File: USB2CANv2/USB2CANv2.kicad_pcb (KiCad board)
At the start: 2 copper layers, 53 parts, among them IC1 MIC5528-3.3YMT-TR, J1 USB_C_Receptacle_USB2.0, J3 Conn_01x04_Pin, SW1 SW_BOOT0, U1 STM32F405RGTx, U2 USBLC6-2P6, U3 MCP2561-E-SN, U4 TLP175A, U5 MCP2561-E-SN, U6 TLP175A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

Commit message: Creating PCB
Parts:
- added J2: Conn_01x06_Pin, IDC:IDC_SMD_3PIN, F.Cu at (96.0, 117.3)
- added J4: Conn_01x02_Pin, Connector_PinHeader_2.54mm:PinHeader_1x02_P2.54mm_Vertical, F.Cu at (54.1, 108.7)
- added J5: Conn_01x02_Pin, Connector_PinHeader_2.54mm:PinHeader_1x02_P2.54mm_Vertical, F.Cu at (54.4, 125.2)
- added R15: 0, Resistor_SMD:R_0402_1005Metric_Pad0.72x0.64mm_HandSolder, F.Cu at (132.5, 57.0)
- added R16: 0, Resistor_SMD:R_0402_1005Metric_Pad0.72x0.64mm_HandSolder, F.Cu at (132.5, 59.0)
- added R17: 0, Resistor_SMD:R_0402_1005Metric_Pad0.72x0.64mm_HandSolder, F.Cu at (132.5, 61.0)
- added R18: 0, Resistor_SMD:R_0402_1005Metric_Pad0.72x0.64mm_HandSolder, F.Cu at (132.5, 63.0)
- added TP1: TestPoint, TestPoint:TestPoint_Pad_1.5x1.5mm, B.Cu at (76.7, 126.0)
- added TP2: TestPoint, TestPoint:TestPoint_Pad_1.5x1.5mm, B.Cu at (69.1, 126.0)
- added TP3: TestPoint, TestPoint:TestPoint_Pad_1.5x1.5mm, B.Cu at (71.6, 126.0)
- added TP4: TestPoint, TestPoint:TestPoint_Pad_1.5x1.5mm, B.Cu at (74.2, 126.0)
- IC1, U3, U4, U5, U6: moved to B.Cu
- J3: value Conn_01x04_Pin -> Conn_01x02_Pin; footprint Connector_PinHeader_2.54mm:PinHeader_1x01_P2.54mm_Vertical -> Connector_PinHeader_2.00mm:PinHeader_1x02_P2.00mm_Vertical
- moved D1 94.5 mm to (59.5, 125.2)
- moved D3 85.0 mm to (49.8, 113.5), turned to -90 degrees
- moved U3 82.8 mm to (66.5, 120.4), turned to 180 degrees
- moved U4 79.6 mm to (54.4, 119.1), turned to 180 degrees
- moved D2 77.6 mm to (59.8, 108.7)
- moved J1 74.3 mm to (44.2, 113.9), turned to -90 degrees
- moved H3 74.1 mm to (96.5, 124.5)
- moved U6 71.4 mm to (54.4, 113.3), turned to 180 degrees
- moved U1 70.3 mm to (73.4, 116.7), turned to 180 degrees
- moved U5 69.5 mm to (66.5, 112.3), turned to 180 degrees
- moved Y2 68.3 mm to (58.9, 119.4)
- moved D4 61.9 mm to (80.3, 108.2)
- moved SW1 56.1 mm to (85.3, 124.5)
- moved H4 54.7 mm to (96.5, 109.2)
- moved IC1 54.6 mm to (82.8, 115.8), turned to 180 degrees
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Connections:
- J3 pad 1: GND -> +5V
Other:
- board outline added: 61 x 20.3 mm

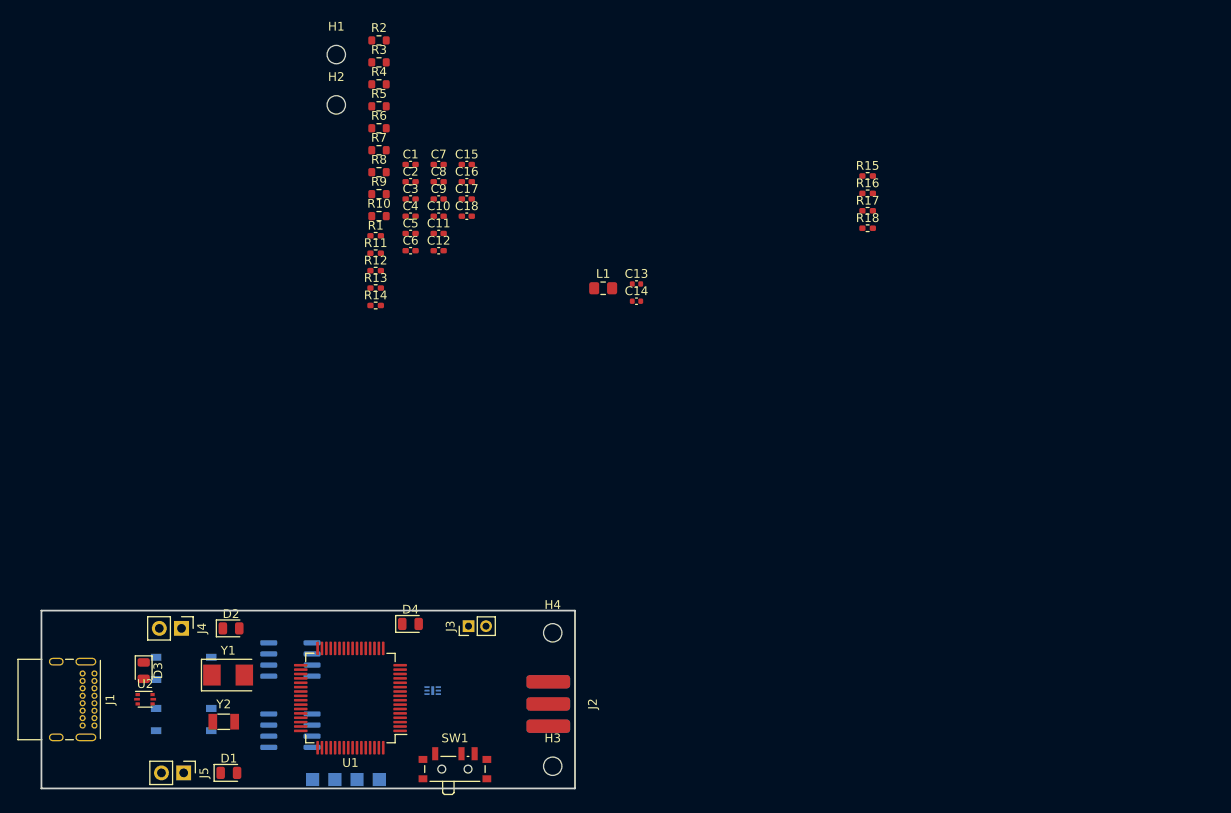
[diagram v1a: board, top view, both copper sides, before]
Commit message: Placement done
Placement done, started routing
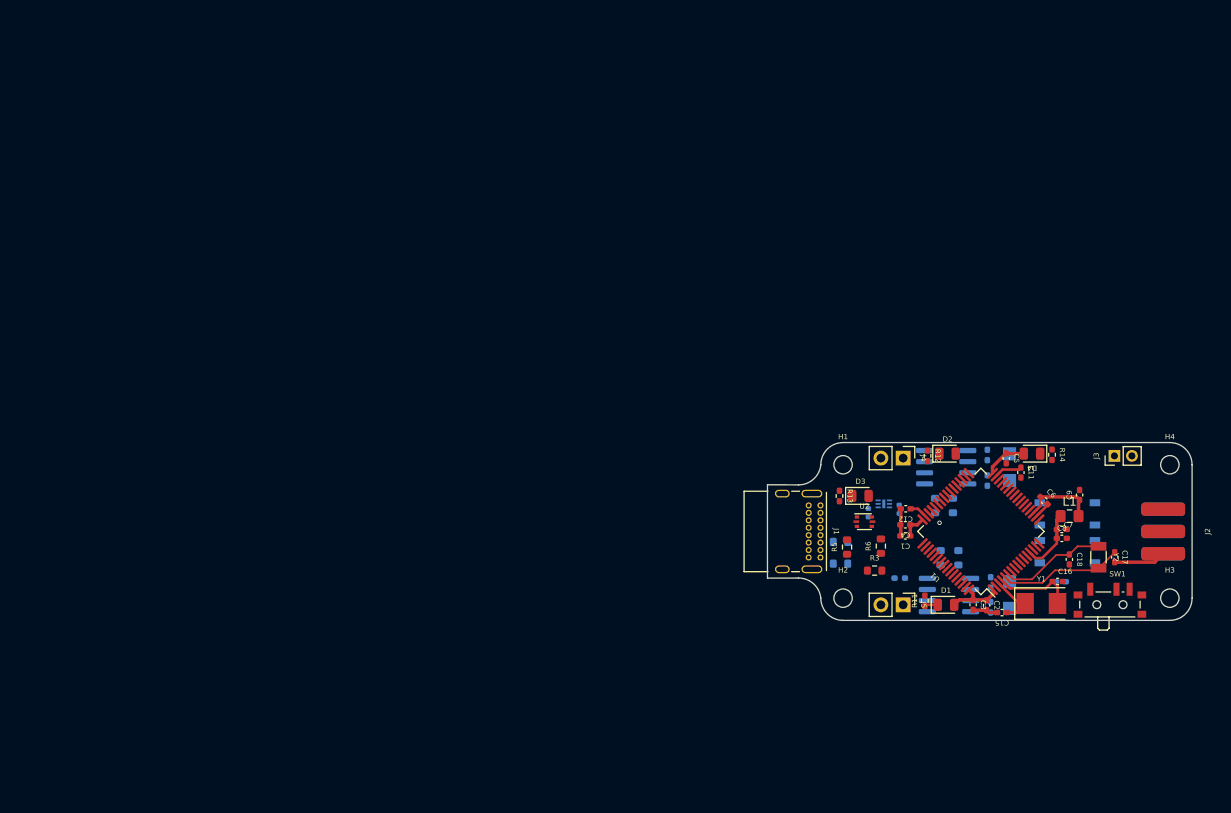
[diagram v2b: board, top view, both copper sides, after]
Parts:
- C10, C13, C14, R1, R10, R15, R16, R17, R18, R2, R4, R7, R8, R9: moved to B.Cu
- moved U4 103.7 mm to (155.3, 95.6), turned to 0 degrees
- moved U6 101.8 mm to (155.3, 99.9)
- moved Y2 101.7 mm to (158.9, 100.6), turned to -90 degrees
- moved Y1 93.3 mm to (152.3, 105.9)
- moved TP3 85.6 mm to (148.7, 88.8)
- moved J1 85.1 mm to (127.1, 94.7)
- moved J4 84.7 mm to (136.6, 89.3)
- moved U2 84.6 mm to (132.1, 96.5)
- moved C17 84.6 mm to (160.7, 100.6), turned to -90 degrees
- moved J5 84.4 mm to (136.6, 106.0)
- moved D3 84.3 mm to (131.7, 93.6), turned to 0 degrees
- moved D2 84.3 mm to (141.6, 88.7)
- moved D1 84.2 mm to (141.5, 106.0)
- moved C7 82.5 mm to (154.7, 97.4)
- moved C10 82.4 mm to (154.6, 103.4), turned to 180 degrees
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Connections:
- C7 pad 1: +3.3V -> +3.3VA
- C8 pad 1: +3.3V -> +3.3VA
- L1 pad 1: +3.3V -> +3.3VA
- U1 pad 13: +3.3V -> +3.3VA
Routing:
- net +3.3V: track 0.00 -> 23.2 mm
- net /HSE_IN: track 0.00 -> 14.2 mm
- net GND: track 0.00 -> 13.9 mm
- net /HSE_OUT: track 0.00 -> 12.2 mm
- net /LSE_OUT: track 0.00 -> 9.21 mm
- net +3.3VA: track 0.00 -> 7.39 mm
- net /LSE_IN: track 0.00 -> 6.44 mm
- net Net-(U1-VCAP_1): track 0.00 -> 3.27 mm
- net Net-(U1-VCAP_2): track 0.00 -> 2.07 mm
- net Net-(D1-K): track 0.00 -> 1.54 mm
- net /SWDIO: vias 0 -> 1
- added copper zone on In1.Cu, net +3.3V
- added copper zone on In2.Cu, net GND
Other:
- board size 61 x 20.3 mm -> 48.5 x 20.3 mm
- copper layers 2 -> 4

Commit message: board routed
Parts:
- C10: moved to F.Cu
- SW1: footprint Button_Switch_SMD:SW_SPDT_PCM12 -> Jumper:SolderJumper-3_P1.3mm_Open_RoundedPad1.0x1.5mm_NumberLabels; moved to B.Cu
- moved SW1 26.7 mm to (133.9, 101.1), turned to 180 degrees
- moved D2 17.9 mm to (141.1, 106.7)
- moved R12 17.6 mm to (138.9, 106.6)
- moved D1 17.1 mm to (141.3, 88.9)
- moved R11 16.7 mm to (138.9, 88.9), turned to -90 degrees
- moved R8 11.2 mm to (151.3, 96.1), turned to 0 degrees
- moved R9 10.7 mm to (151.3, 98.6), turned to 0 degrees
- moved C16 4.48 mm to (158.5, 104.6), turned to 90 degrees
- moved C10 3.82 mm to (150.9, 102.4), turned to 45 degrees
- moved U4 3.60 mm to (154.9, 92.0), turned to 90 degrees
- moved U6 3.32 mm to (154.9, 103.3), turned to -90 degrees
- moved R6 3.20 mm to (130.8, 99.3), turned to 180 degrees
- moved R14 3.05 mm to (152.4, 91.7)
- moved D3 2.80 mm to (134.1, 92.2)
- moved R5 2.72 mm to (130.8, 96.8), turned to 180 degrees
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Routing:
- net GND: track 13.9 -> 88.4 mm, vias 0 -> 30
- net +3.3V: track 23.2 -> 90.3 mm, vias 0 -> 1
- net /SWCLK: track 0.00 -> 32.7 mm, vias 0 -> 2
- net /SWDIO: track 0.00 -> 31.3 mm, vias 1 -> 2
- net /LED_UART: track 0.00 -> 27.4 mm, vias 0 -> 2
- net /CAN2_L: track 0.00 -> 26.7 mm
- net /CAN1_L: track 0.00 -> 25.4 mm
- net /LED_CAN2: track 0.00 -> 24.6 mm, vias 0 -> 2
- net +5V: track 0.00 -> 22.7 mm, vias 0 -> 8
- net Net-(R7-Pad2): track 0.00 -> 19.5 mm
- net /CAN2_TX: track 0.00 -> 19.2 mm, vias 0 -> 1
- net /LED_CAN1: track 0.00 -> 18.7 mm, vias 0 -> 2
- net Net-(J1-CC2): track 0.00 -> 15.3 mm
- net Net-(R10-Pad2): track 0.00 -> 14.2 mm
- net Net-(U1-BOOT0): track 0.00 -> 12.3 mm, vias 0 -> 1
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- added copper zone on In1.Cu, net +5V
- removed copper zone on In1.Cu, net +3.3V
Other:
- board size 48.5 x 20.3 mm -> 48.6 x 20.3 mm

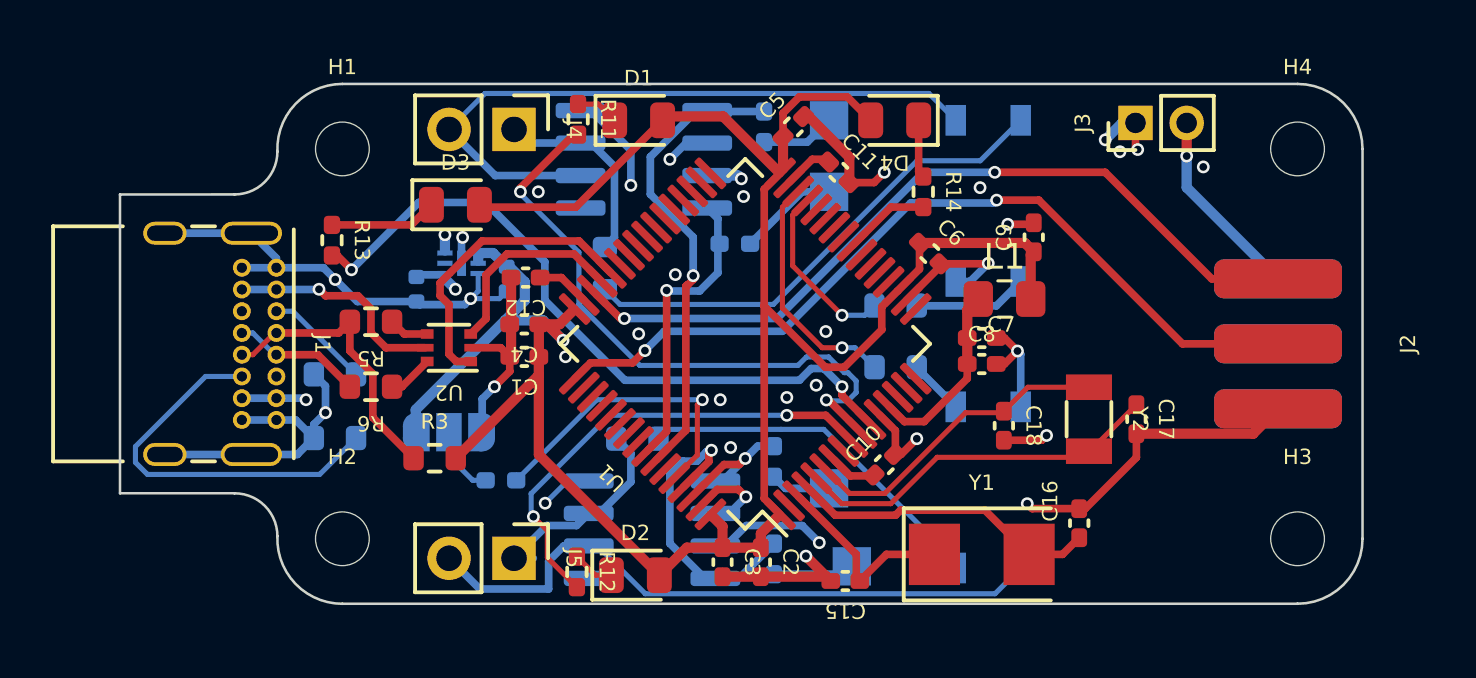
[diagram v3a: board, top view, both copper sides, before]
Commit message: All DRC warnings and errors deleted
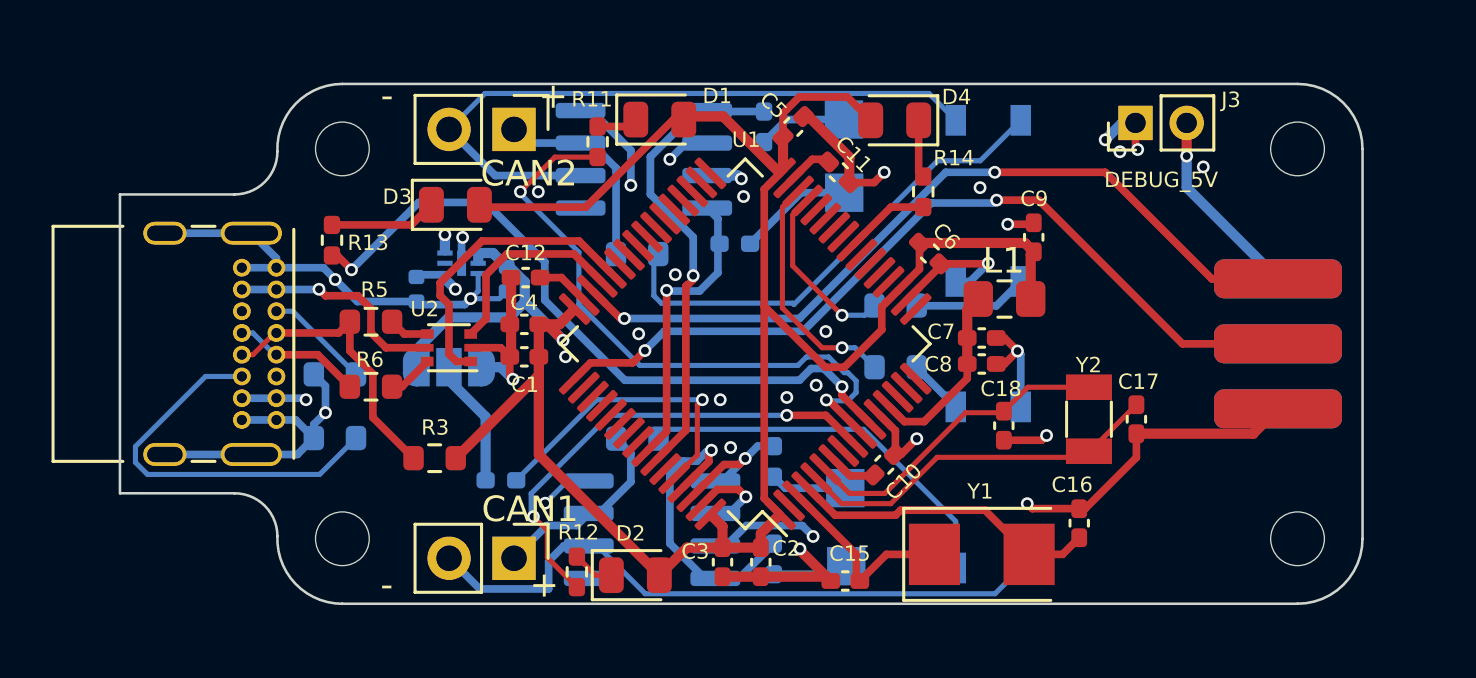
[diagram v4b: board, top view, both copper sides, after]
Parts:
- moved SW1 2.54 mm to (133.9, 98.6)
- moved R7 1.38 mm to (141.2, 94.1), turned to 0 degrees
- moved R11 1.16 mm to (139.7, 89.7)
- moved D1 0.83 mm to (142.1, 88.9)
- moved TP1 0.63 mm to (149.3, 103.3)
- moved TP4 0.59 mm to (149.3, 91.7)
- moved TP3 0.58 mm to (149.3, 88.9)
- moved TP2 0.22 mm to (149.4, 106.3)
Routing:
- net Net-(SW1-B): track 2.77 -> 5.01 mm
- net +3.3V: track 90.3 -> 89.1 mm
- net /CAN1_H: track 9.50 -> 8.48 mm
- net Net-(R10-Pad2): track 14.2 -> 15.1 mm
- net GND: track 88.4 -> 87.6 mm
- net Net-(R15-Pad2): track 2.35 -> 2.98 mm
- net Net-(R18-Pad2): track 3.93 -> 4.51 mm
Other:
- board text added: "+"
- board text added: "-"
- board text added: "CAN1"
- board text added: "CAN2"
- board text added: "DEBUG_5V"

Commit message: Board done
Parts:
- added G***: LOGO, footprints:PGR_srednie, F.Cu at (145.4, 97.6)
- added G***: LOGO, footprints:PGR_male, B.Cu at (144.3, 98.0)
- moved H3 2.44 mm to (164.6, 105.3)
- moved H4 2.44 mm to (164.6, 90.0)
- moved J3 2.19 mm to (158.5, 89.2)
- moved J2 1.94 mm to (164.3, 97.8)
- moved D2 0.84 mm to (142.0, 106.7)
- moved R12 0.84 mm to (139.7, 106.6)
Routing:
- net GND: track 87.6 -> 96.2 mm
- net /SWCLK: track 32.7 -> 30.8 mm
- net /SWDIO: track 31.3 -> 29.5 mm
- net /DEBUG_5V: track 7.58 -> 8.98 mm
- net /LED_CAN1: track 18.7 -> 19.5 mm
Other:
- board size 48.6 x 20.3 mm -> 46.1 x 20.3 mm
- board text added: "Mieszko Celinski Karol Pergol"
- board text added: "USB2CANv2"
